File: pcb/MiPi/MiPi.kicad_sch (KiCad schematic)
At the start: 0 parts

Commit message: Started the schematic design
Almost done with the power circuitry, following the Raspberry Pi Foundation's RP2350 minimal design document.
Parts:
- added C1, C10, C11, C13, C2, C3, C4, C5, C6, C7, C8, C9: 100n, symbol Device:C
- added C12, C15, C16: 4.7u, symbol Device:C
- added C14: C, symbol Device:C
- added L1: 3.3u, symbol Device:L
- added R1: 33, symbol Device:R
- added U1: RP2350_60QFN, RP2350_60QFN_minimal:RP2350-QFN-60-1EP_7x7_P0.4mm_EP3.4x3.4mm_ThermalVias, symbol USER Library:RP2350_60QFN
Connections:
- new net: C14.1, R1.2, U1.46 (VREG_AVDD)
- new net: C16.1, R1.1, U1.49 (VREG_VIN)
- new net: C15.2, C16.2, U1.47 (VREG_PGND)
- new net: L1.2, U1.48 (VREG_LX)
- new net +1V1: C11.1, C12.1, C13.1, C15.1, L1.1, U1.23 (DVDD), U1.39 (DVDD), U1.50 (VREG_FB), U1.6 (DVDD)
- new net +3.3V: C1.1, C10.1, C2.1, C3.1, C4.1, C5.1, C6.1, C7.1, C8.1, C9.1, U1.1 (IOVDD), U1.11 (IOVDD), U1.20 (IOVDD), U1.30 (IOVDD), U1.38 (IOVDD), U1.44 (ADC_AVDD), U1.45 (IOVDD), U1.53 (USB_OTP_VDD), U1.54 (QSPI_IOVDD)
- new net GND: C1.2, C10.2, C11.2, C12.2, C13.2, C14.2, C2.2, C3.2, C4.2, C5.2, C6.2, C7.2, C8.2, C9.2

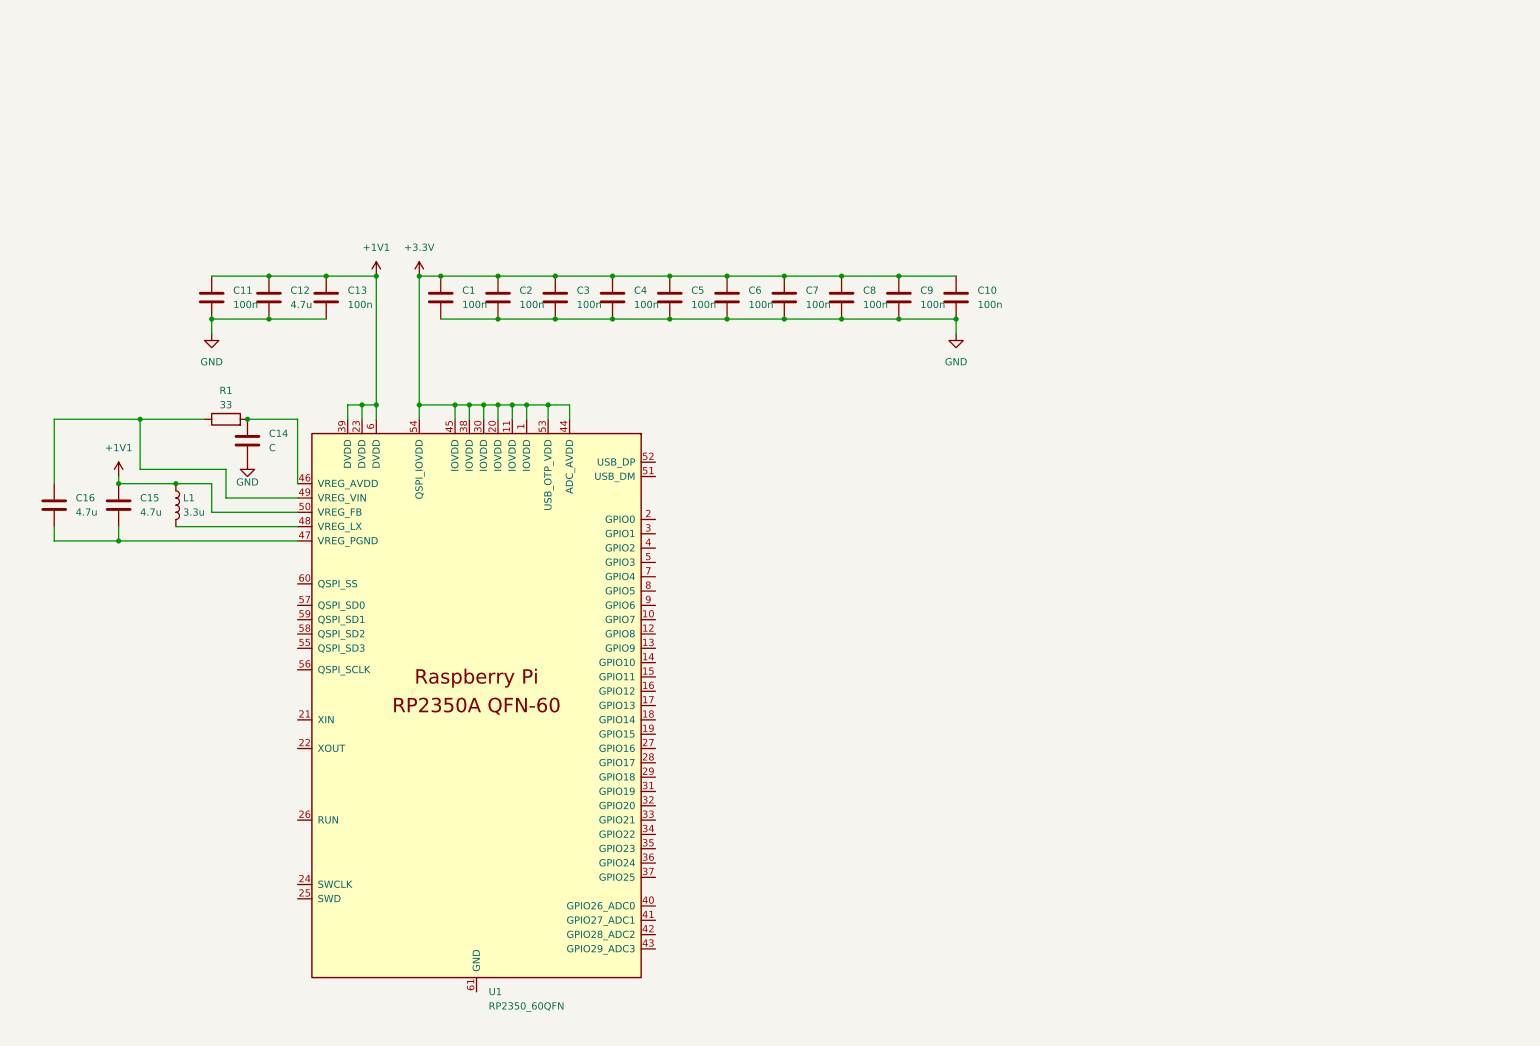
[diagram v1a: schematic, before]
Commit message: MCU chip design done
I finished doing the RP2354A schematic design. To Do: 3v3 regulator, USB connector, check 1v1 circuitry design.
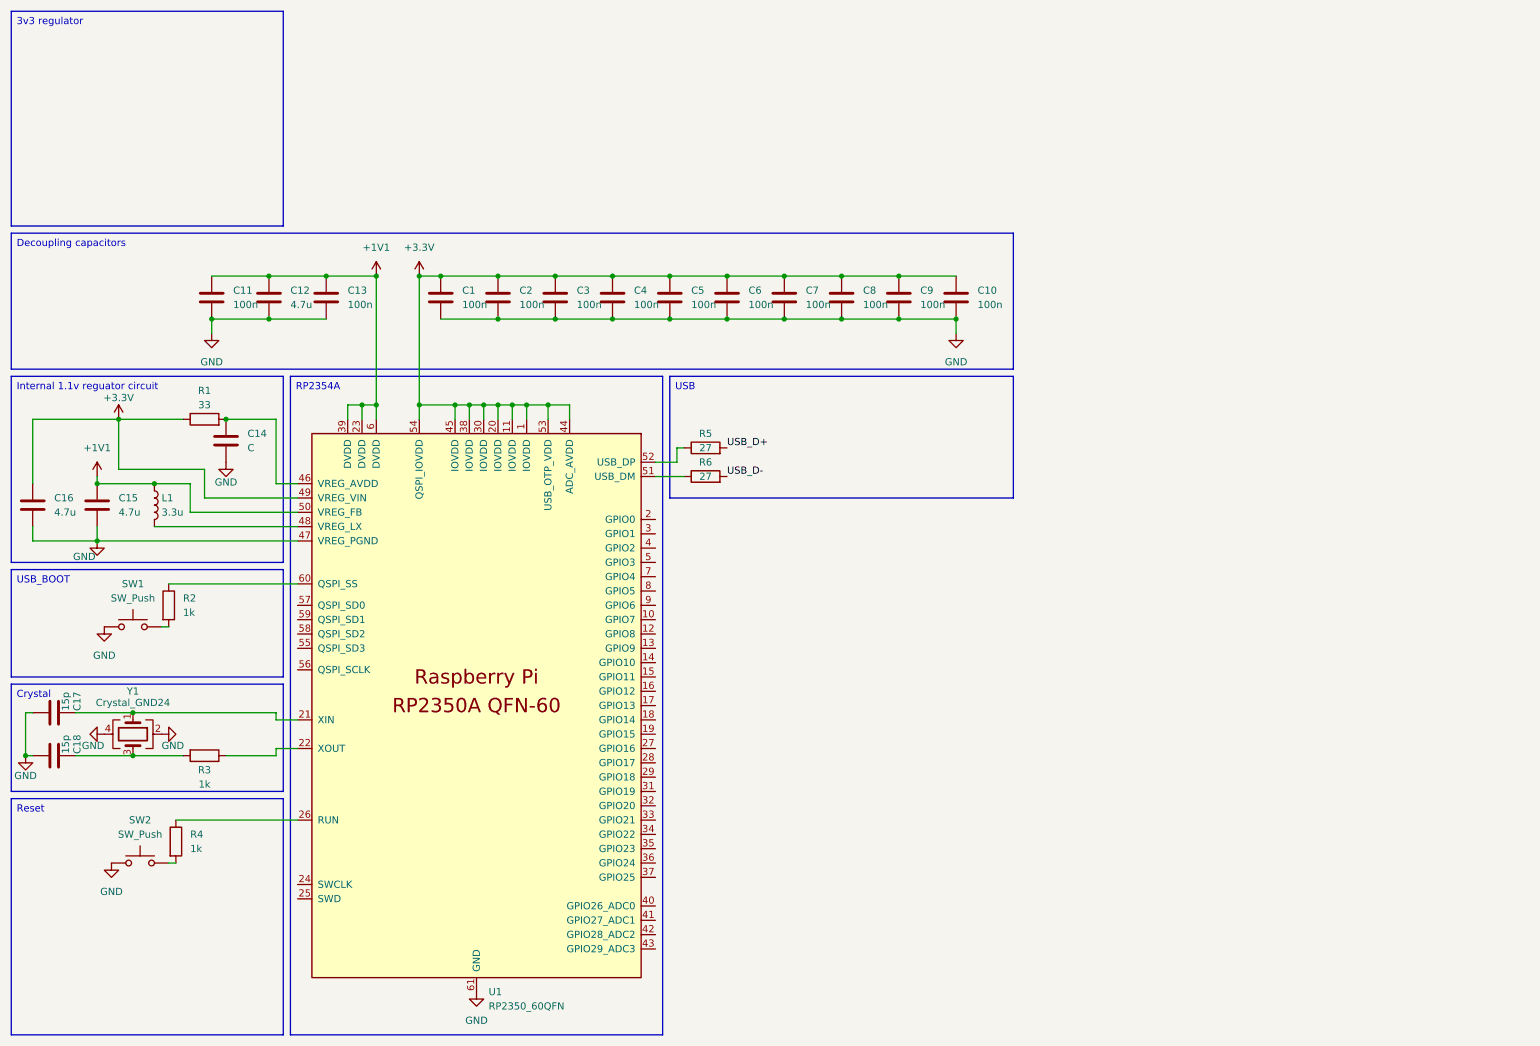
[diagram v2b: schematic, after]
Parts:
- added C17, C18: 15p, symbol Device:C
- added R2, R3, R4: 1k, symbol Device:R
- added R5, R6: 27, symbol Device:R
- added SW1, SW2: SW_Push, symbol Switch:SW_Push
- added Y1: Crystal_GND24, symbol Device:Crystal_GND24
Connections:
- net +3.3V: now also C16.1, R1.1, U1.49 (VREG_VIN)
- net GND: now also C15.2, C16.2, U1.47 (VREG_PGND), U1.61 (GND), C17.2, C18.2, SW1.1, SW2.1, Y1.2, Y1.4
- net at U1.21 (XIN): now also C17.1, Y1.1
- net at U1.22 (XOUT): now also R3.1
- net at U1.26 (RUN): now also R4.1
- net at U1.51 (USB_DM): now also R6.1
- net at U1.52 (USB_DP): now also R5.1
- net at U1.60 (QSPI_SS): now also R2.1
- new net: R2.2, SW1.2
- new net: R4.2, SW2.2
- new net: C18.1, R3.2, Y1.3
- new net USB_D+: R5.2
- new net USB_D-: R6.2
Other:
- moved on the sheet: C14, C15, C16, L1, R1

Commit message: Update MiPi.kicad_sch
1v1 regulator circuitry seems all right, needed to specify a capacitor's value.
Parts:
- C14: value C -> 4.7u
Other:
- company: (none) -> Christian Spînu
- title: (none) -> miPi
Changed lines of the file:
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@@
 	(generator_version "9.0")
 	(paper "A4")
+	(title_block
+		(title "miPi")
+		(rev "0.1")
+		(company "Christian Spînu")
+	)
 	(text_box "USB"
 		(exclude_from_sim no)
@@
 			)
 		)
-		(property "Value" "C"
+		(property "Value" "4.7u"
 			(at 55.88 91.4399 0)
 			(effects

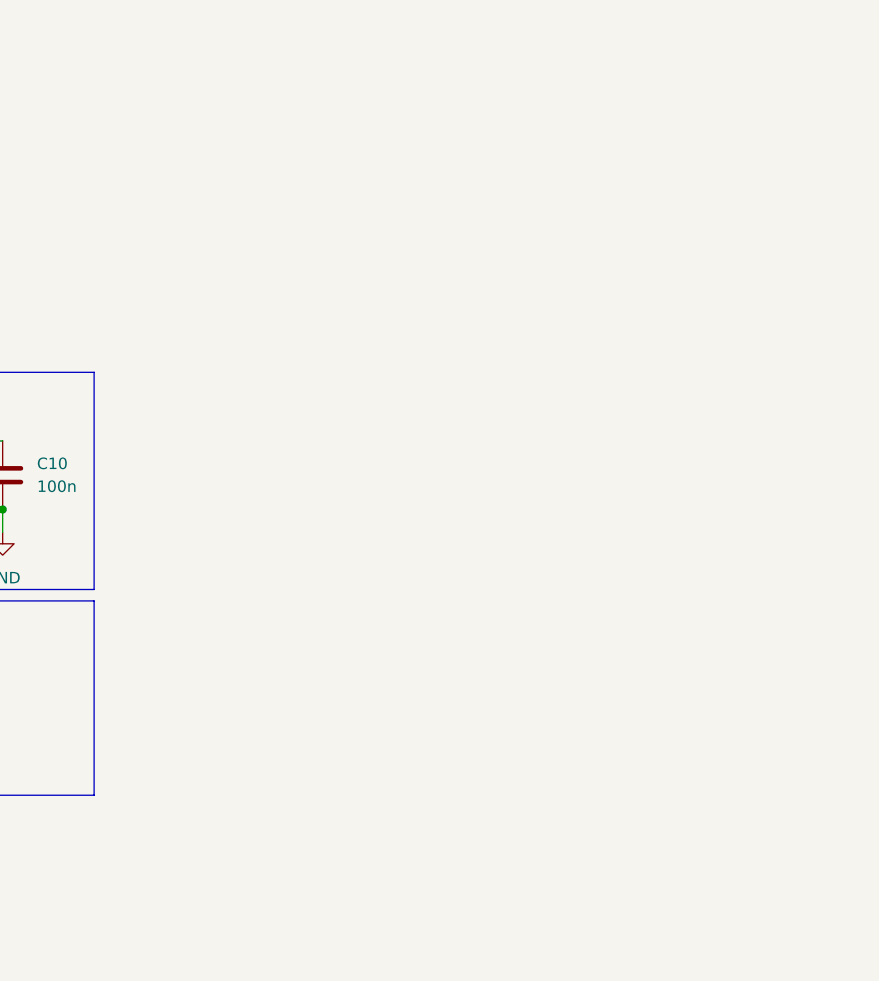
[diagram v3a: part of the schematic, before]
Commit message: Display driving circuit done
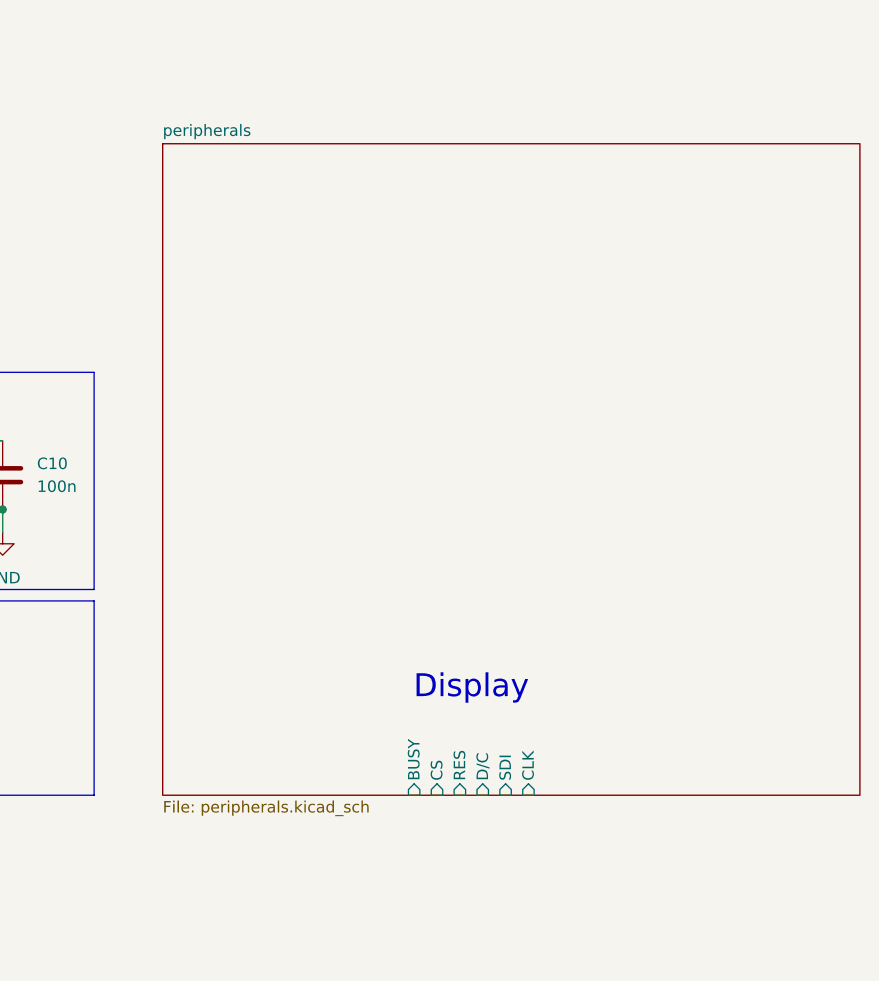
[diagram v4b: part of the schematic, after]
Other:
- added sheet peripherals (peripherals.kicad_sch)
- note added: "Display"
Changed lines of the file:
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@@
 		(company "Christian Spînu")
 	)
+	(text "Display"
+		(exclude_from_sim no)
+		(at 233.68 88.392 0)
+		(effects
+			(font
+				(size 2.54 2.54)
+			)
+		)
+	)
 	(text_box "USB"
 		(exclude_from_sim no)
@@
 				)
 			)
+		)
+	)
+	(sheet
+		(at 199.39 27.94)
+		(size 77.47 72.39)
+		(exclude_from_sim no)
+		(in_bom yes)
+		(on_board yes)
+		(dnp no)
+		(fields_autoplaced yes)
+		(stroke
+			(width 0.1524)
+			(type solid)
+		)
+		(fill
+			(color 0 0 0 0.0000)
+		)
+		(property "Sheetname" "peripherals"
+			(at 199.39 27.2284 0)
+			(effects
+				(font
+					(size 1.27 1.27)
+				)
+				(justify left bottom)
+			)
+		)
+		(property "Sheetfile" "peripherals.kicad_sch"
+			(at 199.39 100.9146 0)
+			(effects
+				(font
+					(size 1.27 1.27)
+				)
+				(justify left top)
+			)
+		)
+		(pin "BUSY" input
+			(at 227.33 100.33 270)
+			(effects
+				(font
+					(size 1.27 1.27)
+				)
+				(justify left)
+			)
+		)
+		(pin "CS" input
+			(at 229.87 100.33 270)
+			(effects
+				(font
+					(size 1.27 1.27)
+				)
+				(justify left)
+			)
+		)
+		(pin "RES" input
+			(at 232.41 100.33 270)
+			(effects
+				(font
+					(size 1.27 1.27)
+				)
+				(justify left)
+			)
+		)
+		(pin "D{slash}C" input
+			(at 234.95 100.33 270)
+			(effects
+				(font
+					(size 1.27 1.27)
+				)
+				(justify left)
+			)
+		)
+		(pin "SDI" input
+			(at 237.49 100.33 270)
+			(effects
+				(font
+					(size 1.27 1.27)
+				)
+				(justify left)
+			)
+		)
+		(pin "CLK" input
+			(at 240.03 100.33 270)
+			(effects
+				(font
+					(size 1.27 1.27)
+				)
+				(justify left)
+			)
+		)
+		(instances
+			(project "MiPi"
+				(path "/b9d145a7-baa8-4ce0-8960-0d6de596954d"
+					(page "2")
+				)
+			)

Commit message: Did RDA5807M, controls and SD circuit schematic
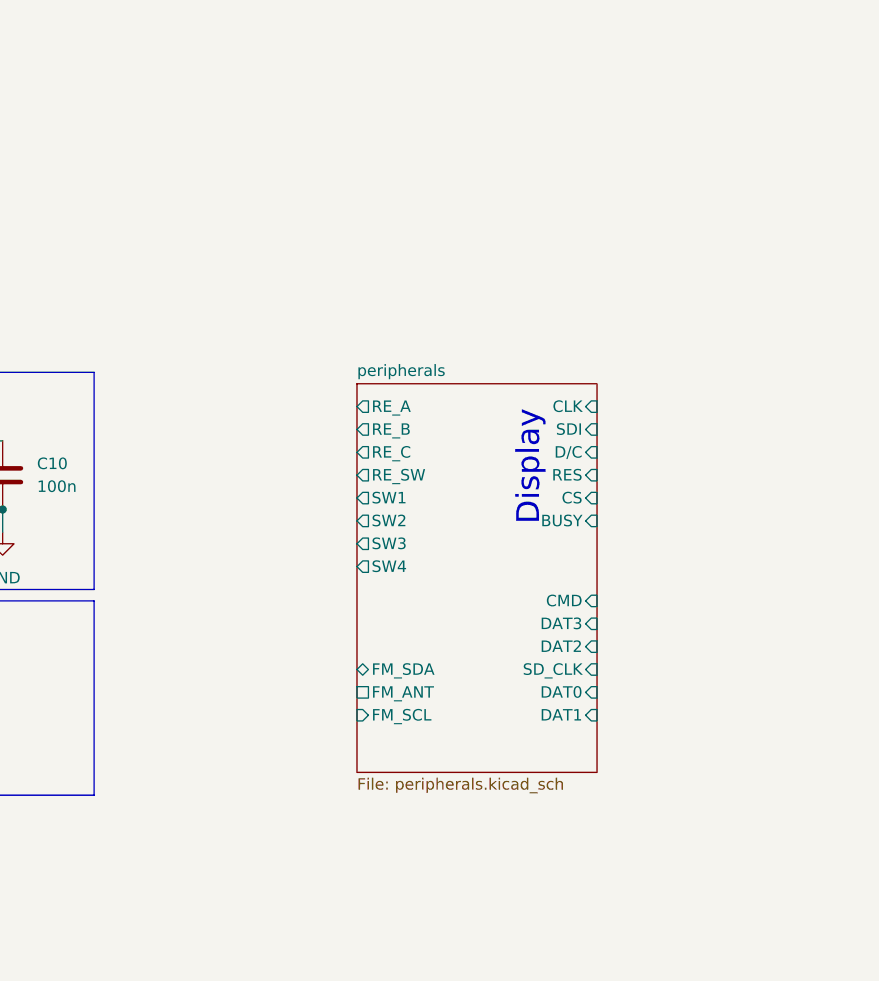
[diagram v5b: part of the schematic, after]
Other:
- sheet peripherals ports: added CMD, DAT0, DAT1, DAT2, DAT3, FM_ANT, FM_SCL, FM_SDA, RE_A, RE_B, RE_C, RE_SW, SD_CLK, SW1, SW2, SW3, SW4; removed none
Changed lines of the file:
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@@
 	(text "Display"
 		(exclude_from_sim no)
-		(at 233.68 88.392 0)
+		(at 240.03 64.008 90)
 		(effects
 			(font
@@
 	)
 	(sheet
-		(at 199.39 27.94)
-		(size 77.47 72.39)
+		(at 220.98 54.61)
+		(size 26.67 43.18)
 		(exclude_from_sim no)
 		(in_bom yes)
@@
 		)
 		(property "Sheetname" "peripherals"
-			(at 199.39 27.2284 0)
+			(at 220.98 53.8984 0)
 			(effects
 				(font
@@
 		)
 		(property "Sheetfile" "peripherals.kicad_sch"
-			(at 199.39 100.9146 0)
+			(at 220.98 98.3746 0)
 			(effects
 				(font
@@
 		)
 		(pin "BUSY" input
-			(at 227.33 100.33 270)
+			(at 247.65 69.85 0)
 			(effects
 				(font
 					(size 1.27 1.27)
 				)
-				(justify left)
+				(justify right)
 			)
 		)
 		(pin "CS" input
-			(at 229.87 100.33 270)
+			(at 247.65 67.31 0)
 			(effects
 				(font
 					(size 1.27 1.27)
 				)
-				(justify left)
+				(justify right)
 			)
 		)
 		(pin "RES" input
-			(at 232.41 100.33 270)
+			(at 247.65 64.77 0)
 			(effects
 				(font
 					(size 1.27 1.27)
 				)
-				(justify left)
+				(justify right)
 			)
 		)
 		(pin "D{slash}C" input
-			(at 234.95 100.33 270)
+			(at 247.65 62.23 0)
 			(effects
 				(font
 					(size 1.27 1.27)
 				)
-				(justify left)
+				(justify right)
 			)
 		)
 		(pin "SDI" input
-			(at 237.49 100.33 270)
+			(at 247.65 59.69 0)
 			(effects
 				(font
 					(size 1.27 1.27)
 				)
-				(justify left)
+				(justify right)
 			)
 		)
 		(pin "CLK" input
-			(at 240.03 100.33 270)
+			(at 247.65 57.15 0)
+			(effects
+				(font
+					(size 1.27 1.27)
+				)
+				(justify right)
+			)
+		)
+		(pin "CMD" input
+			(at 247.65 78.74 0)
+			(effects
+				(font
+					(size 1.27 1.27)
+				)
+				(justify right)
+			)
+		)
+		(pin "DAT3" input
+			(at 247.65 81.28 0)
+			(effects
+				(font
+					(size 1.27 1.27)
+				)
+				(justify right)
+			)
+		)
+		(pin "DAT2" input
+			(at 247.65 83.82 0)
+			(effects
+				(font
+					(size 1.27 1.27)
+				)
+				(justify right)
+			)
+		)
+		(pin "SD_CLK" input
+			(at 247.65 86.36 0)
+			(effects
+				(font
+					(size 1.27 1.27)
+				)
+				(justify right)
+			)
+		)
+		(pin "DAT0" input
+			(at 247.65 88.9 0)
+			(effects
+				(font
+					(size 1.27 1.27)
+				)
+				(justify right)
+			)
+		)
+		(pin "DAT1" input
+			(at 247.65 91.44 0)
+			(effects
+				(font
+					(size 1.27 1.27)
+				)
+				(justify right)
+			)
+		)
+		(pin "RE_B" output
+			(at 220.98 59.69 180)
+			(effects
+				(font
+					(size 1.27 1.27)
+				)
+				(justify left)
+			)
+		)
+		(pin "SW1" output
+			(at 220.98 67.31 180)
+			(effects
+				(font
+					(size 1.27 1.27)
+				)
+				(justify left)
+			)
+		)
+		(pin "RE_A" output
+			(at 220.98 57.15 180)
+			(effects
+				(font
+					(size 1.27 1.27)
+				)
+				(justify left)
+			)
+		)
+		(pin "RE_SW" output
+			(at 220.98 64.77 180)
+			(effects
+				(font
+					(size 1.27 1.27)
+				)
+				(justify left)
+			)
+		)
+		(pin "RE_C" output
+			(at 220.98 62.23 180)
+			(effects
+				(font
+					(size 1.27 1.27)
+				)
+				(justify left)
+			)
+		)
+		(pin "SW2" output
+			(at 220.98 69.85 180)
+			(effects
+				(font
+					(size 1.27 1.27)
+				)
+				(justify left)
+			)
+		)
+		(pin "SW4" output
+			(at 220.98 74.93 180)
+			(effects
+				(font
+					(size 1.27 1.27)
+				)
+				(justify left)
+			)
+		)
+		(pin "SW3" output
+			(at 220.98 72.39 180)
+			(effects
+				(font
+					(size 1.27 1.27)
+				)
+				(justify left)
+			)
+		)
+		(pin "FM_SCL" input
+			(at 220.98 91.44 180)
+			(effects
+				(font
+					(size 1.27 1.27)
+				)
+				(justify left)
+			)
+		)
+		(pin "FM_ANT" passive
+			(at 220.98 88.9 180)
+			(effects
+				(font
+					(size 1.27 1.27)
+				)
+				(justify left)
+			)
+		)
+		(pin "FM_SDA" bidirectional
+			(at 220.98 86.36 180)
 			(effects
 				(font
